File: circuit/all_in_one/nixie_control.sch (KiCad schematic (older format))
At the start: 0 parts

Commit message: [All in one]Construct mode circuits
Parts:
- added C? (x2): C, symbol C
- added IC?: ATMEGA328P-A, TQFP32, symbol ATMEGA328P-A
- added P?: CONN_01X08, symbol CONN_01X08
- added P?: CONN_01X12, symbol CONN_01X12
- added P?: CONN_02X04, symbol CONN_02X04
- added R? (x3): R, symbol R
- added SW? (x2): SW_PUSH, symbol SW_PUSH
- added U?: K155ID1, symbol K155ID1
- added U?: HEF4028, symbol HEF4028
- added U? (x4): TLP521, symbol TLP521
- added Y?: Crystal, symbol Crystal
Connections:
- net 170V: now also R?.2
- net 5V: now also IC?.18 (AVCC), IC?.20 (AREF), IC?.4 (VCC), IC?.6 (VCC), P?.5 (P5), P?.6 (P6), R?.2, SW?.1, U?.16 (VDD), U?.5 (Vcc)
- net GND: now also C?.2, C?.2, IC?.21 (GND), IC?.3 (GND), IC?.5 (GND), P?.7 (P7), P?.8 (P8), R?.1, SW?.1, U?.12 (Gnd), U?.8 (VSS)
- new net: P?.9 (P9), U?.1 (8)
- new net: P?.8 (P8), U?.10 (7)
- new net: P?.7 (P7), U?.11 (6)
- new net: P?.5 (P5), U?.13 (4)
- new net: P?.6 (P6), U?.14 (5)
- new net: P?.2 (P2), U?.15 (1)
- new net: P?.1 (P1), U?.16 (0)
- new net: P?.10 (P10), U?.2 (9)
- new net: P?.3 (P3), U?.8 (2)
- new net: P?.4 (P4), U?.9 (3)
- new net: U?.1 (Y4), U?.3 (A)
- new net: U?.1 (A), U?.14 (Y1)
- new net: U?.1 (A), U?.15 (Y3)
- new net: U?.2 (Y2), U?.3 (A)
- new net: U?.3 (A), U?.3 (Y0)
- new net: U?.1 (A), U?.4 (Y7)
- new net: U?.1 (A), U?.6 (Y5)
- new net: U?.3 (A), U?.7 (Y6)
- new net: U?.2 (C), U?.2 (C), U?.2 (C), U?.2 (C), U?.4 (C), U?.4 (C), U?.4 (C), U?.4 (C)
- new net: P?.6 (P6), U?.5 (E)
- new net: R?.1, U?.6 (C), U?.6 (C), U?.6 (C), U?.6 (C), U?.8 (C), U?.8 (C), U?.8 (C), U?.8 (C)
- new net: P?.5 (P5), U?.7 (E)
- new net: P?.8 (P8), U?.5 (E)
- new net: P?.7 (P7), U?.7 (E)
- new net: P?.2 (P2), U?.5 (E)
- new net: P?.1 (P1), U?.7 (E)
- new net: P?.4 (P4), U?.5 (E)
- new net: P?.3 (P3), U?.7 (E)
- new net Crystal1: C?.1, IC?.7 ((PCINT6/XTAL1/TOSC1)PB6), Y?.1
- new net Ctystal2: C?.1, IC?.8 ((PCINT7/XTAL2/TOSC2)PB7), Y?.2
- new net Digit_A0: IC?.12 ((PCINT0/CLKO/ICP1)PB0), U?.10 (A0)
- new net Digit_A1: IC?.11 ((PCINT23/AIN1)PD7), U?.13 (A1)
- new net Digit_A2: IC?.10 ((PCINT22/OC0A/AIN0)PD6), U?.12 (A2)
- new net Digit_A3: IC?.9 ((PCINT21/OC0B/T1)PD5), U?.11 (A3)
- new net Font_A: U?.3 (A)
- new net Font_B: U?.6 (B)
- new net Font_C: U?.7 (C)
- new net Font_D: IC?.14 ((PCINT2/OC1B/~SS~)PB2), U?.4 (D)
- new net I2C_SCL: IC?.28 ((PCINT13/SCL/ADC5)PC5)
- new net I2C_SDA: IC?.27 ((PCINT12/SDA/ADC4)PC4)
- new net Mode_button: IC?.32 ((PCINT18/INT0)PD2), R?.2, SW?.2
- new net Reset: IC?.29 ((PCINT14/~RESET~)PC6), R?.1, SW?.2
- new net USART_RX: IC?.30 ((PCINT16/RXD)PD0), P?.1 (P1), P?.2 (P2)
- new net USART_TX: IC?.31 ((PCINT17/TXD)PD1), P?.3 (P3), P?.4 (P4)
- no-connect marks 0 -> 2

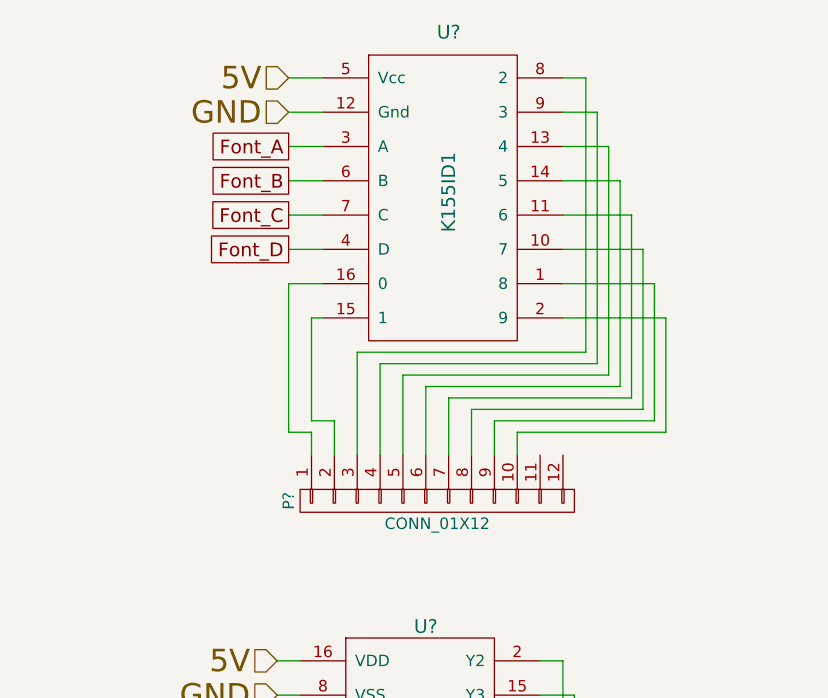
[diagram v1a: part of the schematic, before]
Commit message: [All in one circuit]Add DS1307
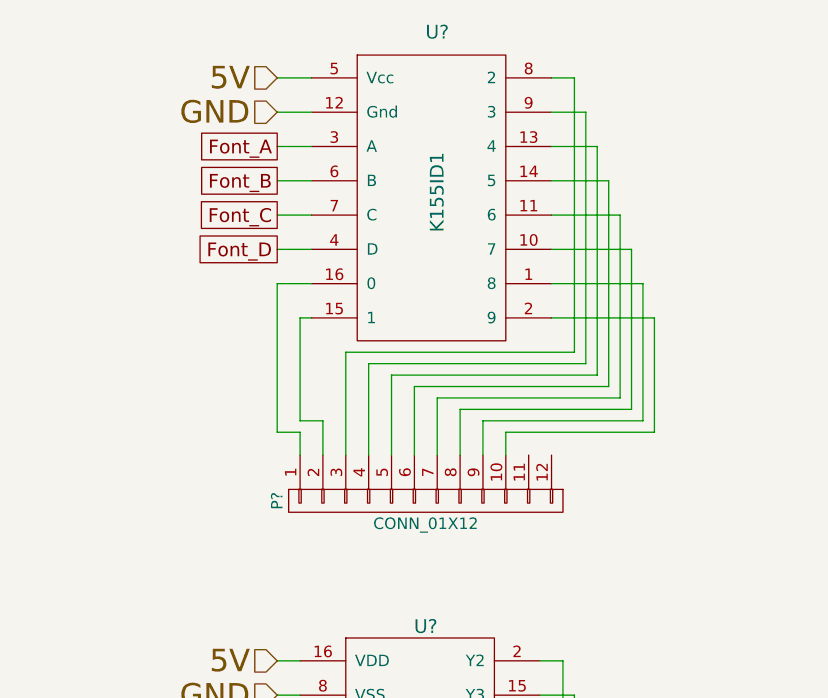
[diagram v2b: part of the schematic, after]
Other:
- moved on the sheet: P?, U?
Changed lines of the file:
@@
 L K155ID1 U?
 U 1 1 5646D245
-P 5350 1750
-F 0 "U?" H 5350 2500 60  0000 C CNN
-F 1 "K155ID1" V 5350 1800 60  0000 C CNN
-F 2 "" H 5350 2500 60  0000 C CNN
-F 3 "" H 5350 2500 60  0000 C CNN
-	1    5350 1750
+P 5300 1750
+F 0 "U?" H 5300 2500 60  0000 C CNN
+F 1 "K155ID1" V 5300 1800 60  0000 C CNN
+F 2 "" H 5300 2500 60  0000 C CNN
+F 3 "" H 5300 2500 60  0000 C CNN
+	1    5300 1750
 	1    0    0    -1
 $EndComp
@@
 	0    1    1    0
 $EndComp
-Text HLabel 4650 1200 0    98   Input ~ 0
+Text HLabel 4600 1200 0    98   Input ~ 0
 5V
-Text HLabel 4650 1350 0    98   Input ~ 0
+Text HLabel 4600 1350 0    98   Input ~ 0
 GND
-Text GLabel 4650 1500 0    60   UnSpc ~ 0
+Text GLabel 4600 1500 0    60   UnSpc ~ 0
 Font_A
-Text GLabel 4650 1650 0    60   UnSpc ~ 0
+Text GLabel 4600 1650 0    60   UnSpc ~ 0
 Font_B
-Text GLabel 4650 1800 0    60   UnSpc ~ 0
+Text GLabel 4600 1800 0    60   UnSpc ~ 0
 Font_C
-Text GLabel 4650 1950 0    60   UnSpc ~ 0
+Text GLabel 4600 1950 0    60   UnSpc ~ 0
 Font_D
 $Comp
 L CONN_01X12 P?
 U 1 1 56472490
-P 5300 3050
-F 0 "P?" H 5300 3700 50  0000 C CNN
-F 1 "CONN_01X12" V 5400 3050 50  0000 C CNN
-F 2 "" H 5300 3050 60  0000 C CNN
-F 3 "" H 5300 3050 60  0000 C CNN
-	1    5300 3050
+P 5250 3050
+F 0 "P?" H 5250 3700 50  0000 C CNN
+F 1 "CONN_01X12" V 5350 3050 50  0000 C CNN
+F 2 "" H 5250 3050 60  0000 C CNN
+F 3 "" H 5250 3050 60  0000 C CNN
+	1    5250 3050
 	0    -1   1    0
 $EndComp
@@
 	5550 6800 5550 6900
 Wire Wire Line
-	4650 1200 4800 1200
-Wire Wire Line
-	4650 1350 4800 1350
-Wire Wire Line
-	4650 1500 4800 1500
-Wire Wire Line
-	4650 1650 4800 1650
-Wire Wire Line
-	4650 1800 4800 1800
-Wire Wire Line
-	4650 1950 4800 1950
-Wire Wire Line
-	4800 2100 4650 2100
-Wire Wire Line
-	4650 2100 4650 2750
-Wire Wire Line
-	4650 2750 4750 2750
-Wire Wire Line
-	4750 2750 4750 2850
-Wire Wire Line
-	4750 2700 4850 2700
-Wire Wire Line
-	4850 2700 4850 2850
-Wire Wire Line
-	5850 1200 5950 1200
-Wire Wire Line
-	5950 1200 5950 2400
-Wire Wire Line
-	5950 2400 4950 2400
-Wire Wire Line
-	4950 2400 4950 2850
-Wire Wire Line
-	5050 2850 5050 2450
-Wire Wire Line
-	5050 2450 6000 2450
-Wire Wire Line
-	6000 2450 6000 1350
-Wire Wire Line
-	6000 1350 5850 1350
-Wire Wire Line
-	5850 1500 6050 1500
-Wire Wire Line
-	6050 1500 6050 2500
-Wire Wire Line
-	6050 2500 5150 2500
-Wire Wire Line
-	5150 2500 5150 2850
-Wire Wire Line
-	5850 1650 6100 1650
-Wire Wire Line
-	6100 1650 6100 2550
-Wire Wire Line
-	6100 2550 5250 2550
-Wire Wire Line
-	5250 2550 5250 2850
-Wire Wire Line
-	5850 1800 6150 1800
-Wire Wire Line
-	6150 1800 6150 2600
-Wire Wire Line
-	6150 2600 5350 2600
-Wire Wire Line
-	5350 2600 5350 2850
-Wire Wire Line
-	5850 1950 6200 1950
-Wire Wire Line
-	6200 1950 6200 2650
-Wire Wire Line
-	6200 2650 5450 2650
-Wire Wire Line
-	5450 2650 5450 2850
-Wire Wire Line
-	5850 2100 6250 2100
-Wire Wire Line
-	6250 2100 6250 2700
-Wire Wire Line
-	6250 2700 5550 2700
-Wire Wire Line
-	5550 2700 5550 2850
-Wire Wire Line
-	5650 2850 5650 2750
-Wire Wire Line
-	5650 2750 6300 2750
-Wire Wire Line
-	6300 2750 6300 2250
-Wire Wire Line
-	6300 2250 5850 2250
-Wire Wire Line
-	4800 2250 4750 2250
-Wire Wire Line
-	4750 2250 4750 2700
+	4600 1200 4750 1200
+Wire Wire Line
+	4600 1350 4750 1350
+Wire Wire Line
+	4600 1500 4750 1500
+Wire Wire Line
+	4600 1650 4750 1650
+Wire Wire Line
+	4600 1800 4750 1800
+Wire Wire Line
+	4600 1950 4750 1950
+Wire Wire Line
+	4750 2100 4600 2100
+Wire Wire Line
+	4600 2100 4600 2750
+Wire Wire Line
+	4600 2750 4700 2750
+Wire Wire Line
+	4700 2750 4700 2850
+Wire Wire Line
+	4700 2700 4800 2700
+Wire Wire Line
+	4800 2700 4800 2850
+Wire Wire Line
+	5800 1200 5900 1200
+Wire Wire Line
+	5900 1200 5900 2400
+Wire Wire Line
+	5900 2400 4900 2400
+Wire Wire Line
+	4900 2400 4900 2850
+Wire Wire Line
+	5000 2850 5000 2450
+Wire Wire Line
+	5000 2450 5950 2450
+Wire Wire Line
+	5950 2450 5950 1350
+Wire Wire Line
+	5950 1350 5800 1350
+Wire Wire Line
+	5800 1500 6000 1500
+Wire Wire Line
+	6000 1500 6000 2500
+Wire Wire Line
+	6000 2500 5100 2500
+Wire Wire Line
+	5100 2500 5100 2850
+Wire Wire Line
+	5800 1650 6050 1650
+Wire Wire Line
+	6050 1650 6050 2550
+Wire Wire Line
+	6050 2550 5200 2550
+Wire Wire Line
+	5200 2550 5200 2850
+Wire Wire Line
+	5800 1800 6100 1800
+Wire Wire Line
+	6100 1800 6100 2600
+Wire Wire Line
+	6100 2600 5300 2600
+Wire Wire Line
+	5300 2600 5300 2850
+Wire Wire Line
+	5800 1950 6150 1950
+Wire Wire Line
+	6150 1950 6150 2650
+Wire Wire Line
+	6150 2650 5400 2650
+Wire Wire Line
+	5400 2650 5400 2850
+Wire Wire Line
+	5800 2100 6200 2100
+Wire Wire Line
+	6200 2100 6200 2700
+Wire Wire Line
+	6200 2700 5500 2700
+Wire Wire Line
+	5500 2700 5500 2850
+Wire Wire Line
+	5600 2850 5600 2750
+Wire Wire Line
+	5600 2750 6250 2750
+Wire Wire Line
+	6250 2750 6250 2250
+Wire Wire Line
+	6250 2250 5800 2250
+Wire Wire Line
+	4750 2250 4700 2250
+Wire Wire Line
+	4700 2250 4700 2700
 Wire Wire Line
 	9850 1450 10000 1450

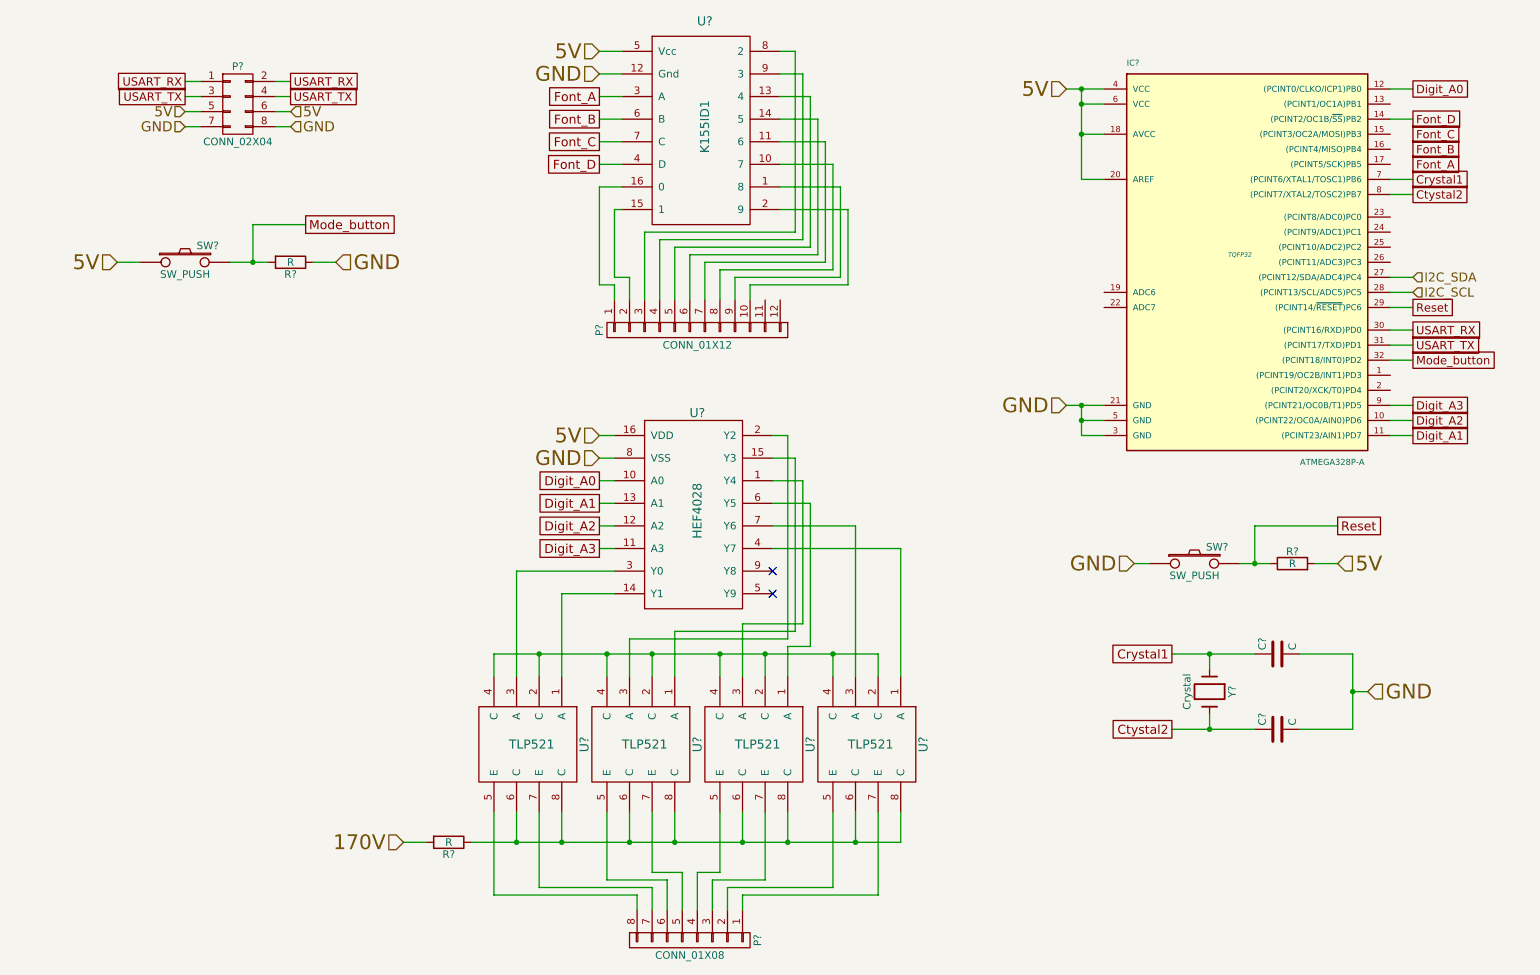
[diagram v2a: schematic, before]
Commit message: [All in one circuit]Arrange the USART pin
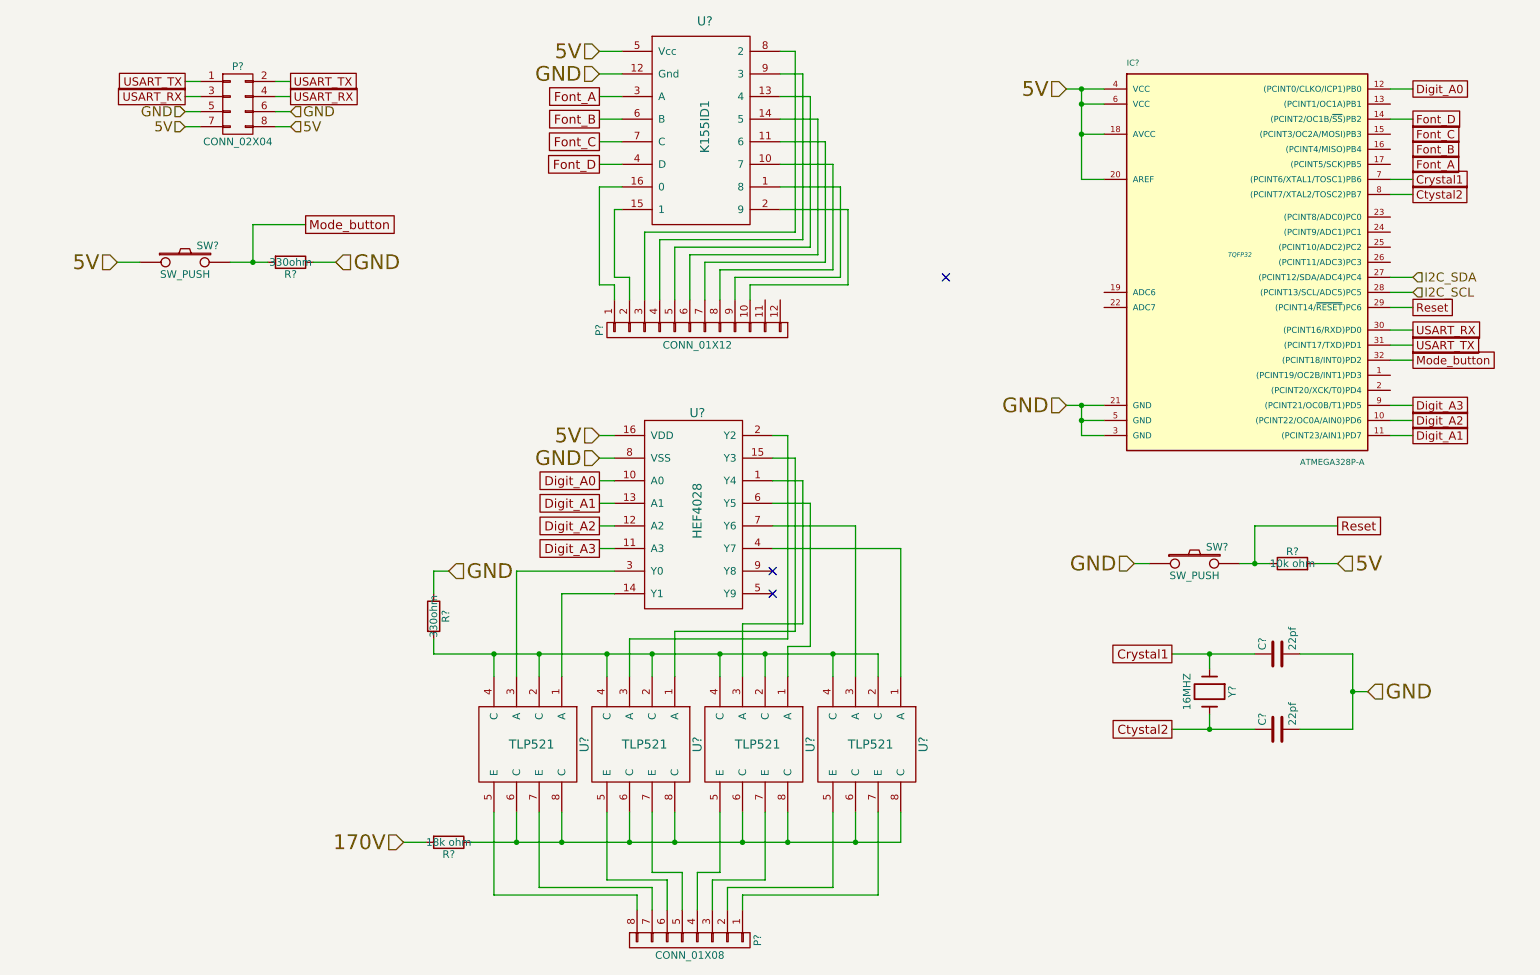
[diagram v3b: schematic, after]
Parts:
- added R?: 330ohm, symbol R
- C? (x2): value C -> 22pf
- R?: value R -> 10k ohm
- R?: value R -> 18k ohm
- R?: value R -> 330ohm
- Y?: value Crystal -> 16MHZ
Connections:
- net 5V: now also P?.7 (P7), P?.8 (P8); no longer P?.5 (P5), P?.6 (P6)
- net GND: now also P?.5 (P5), P?.6 (P6), R?.1; no longer P?.7 (P7), P?.8 (P8)
- net USART_RX: now also P?.3 (P3), P?.4 (P4); no longer P?.1 (P1), P?.2 (P2)
- net USART_TX: now also P?.1 (P1), P?.2 (P2); no longer P?.3 (P3), P?.4 (P4)
- net at U?.2 (C), U?.2 (C), U?.2 (C)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: now also R?.2
- no-connect marks 2 -> 3
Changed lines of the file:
@@
 P 9200 4600
 F 0 "R?" V 9280 4600 50  0000 C CNN
-F 1 "R" V 9200 4600 50  0000 C CNN
+F 1 "10k ohm" V 9200 4600 50  0000 C CNN
 F 2 "" V 9130 4600 30  0000 C CNN
 F 3 "" H 9200 4600 30  0000 C CNN
@@
 P 9100 5200
 F 0 "C?" H 9125 5300 50  0000 L CNN
-F 1 "C" H 9125 5100 50  0000 L CNN
+F 1 "22pf" H 9125 5100 50  0000 L CNN
 F 2 "" H 9138 5050 30  0000 C CNN
 F 3 "" H 9100 5200 60  0000 C CNN
@@
 P 9100 5700
 F 0 "C?" H 9125 5800 50  0000 L CNN
-F 1 "C" H 9125 5600 50  0000 L CNN
+F 1 "22pf" H 9125 5600 50  0000 L CNN
 F 2 "" H 9138 5550 30  0000 C CNN
 F 3 "" H 9100 5700 60  0000 C CNN
@@
 P 8650 5450
 F 0 "Y?" H 8650 5600 50  0000 C CNN
-F 1 "Crystal" H 8650 5300 50  0000 C CNN
+F 1 "16MHZ" H 8650 5300 50  0000 C CNN
 F 2 "" H 8650 5450 60  0000 C CNN
 F 3 "" H 8650 5450 60  0000 C CNN
@@
 P 3600 6450
 F 0 "R?" V 3680 6450 50  0000 C CNN
-F 1 "R" V 3600 6450 50  0000 C CNN
+F 1 "18k ohm" V 3600 6450 50  0000 C CNN
 F 2 "" V 3530 6450 30  0000 C CNN
 F 3 "" H 3600 6450 30  0000 C CNN
@@
 	3900 5350 3900 5200
 Wire Wire Line
-	3900 5200 6450 5200
+	3500 5200 6450 5200
 Wire Wire Line
 	6450 5200 6450 5350
@@
 	1    0    0    -1
 $EndComp
+Text HLabel 1850 1700 0    67   Input ~ 0
+5V
 Text HLabel 1850 1600 0    67   Input ~ 0
+GND
+Wire Wire Line
+	1850 1600 1950 1600
+Text HLabel 2550 1700 2    67   Input ~ 0
 5V
-Text HLabel 1850 1700 0    67   Input ~ 0
-GND
-Wire Wire Line
-	1850 1600 1950 1600
 Text HLabel 2550 1600 2    67   Input ~ 0
-5V
-Text HLabel 2550 1700 2    67   Input ~ 0
 GND
 Wire Wire Line
 	2450 1600 2550 1600
+Text GLabel 1850 1500 0    55   UnSpc ~ 0
+USART_RX
 Text GLabel 1850 1400 0    55   UnSpc ~ 0
+USART_TX
+Text GLabel 2550 1500 2    55   UnSpc ~ 0
 USART_RX
-Text GLabel 1850 1500 0    55   UnSpc ~ 0
-USART_TX
 Text GLabel 2550 1400 2    55   UnSpc ~ 0
-USART_RX
-Text GLabel 2550 1500 2    55   UnSpc ~ 0
 USART_TX
 Wire Wire Line
@@
 P 2550 2600
 F 0 "R?" V 2630 2600 50  0000 C CNN
-F 1 "R" V 2550 2600 50  0000 C CNN
+F 1 "330ohm" V 2550 2600 50  0000 C CNN
 F 2 "" V 2480 2600 30  0000 C CNN
 F 3 "" H 2550 2600 30  0000 C CNN
@@
 	2300 2350 2650 2350
 Connection ~ 2300 2600
+NoConn ~ 6900 2700
+$Comp
+L R R?
+U 1 1 56483273
+P 3500 4950
+F 0 "R?" V 3580 4950 50  0000 C CNN
+F 1 "330ohm" V 3500 4950 50  0000 C CNN
+F 2 "" V 3430 4950 30  0000 C CNN
+F 3 "" H 3500 4950 30  0000 C CNN
+	1    3500 4950
+	1    0    0    -1
+$EndComp
+Text HLabel 3600 4650 2    98   Input ~ 0
+GND
+Wire Wire Line
+	3600 4650 3500 4650
+Wire Wire Line
+	3500 4650 3500 4800
+Wire Wire Line
+	3500 5100 3500 5200
+Connection ~ 3900 5200
 $EndSCHEMATC
